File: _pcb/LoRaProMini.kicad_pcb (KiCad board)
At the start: 2 copper layers, 90 x 32 mm, 23 parts, among them U1 MCP1700-3302E_SOT23

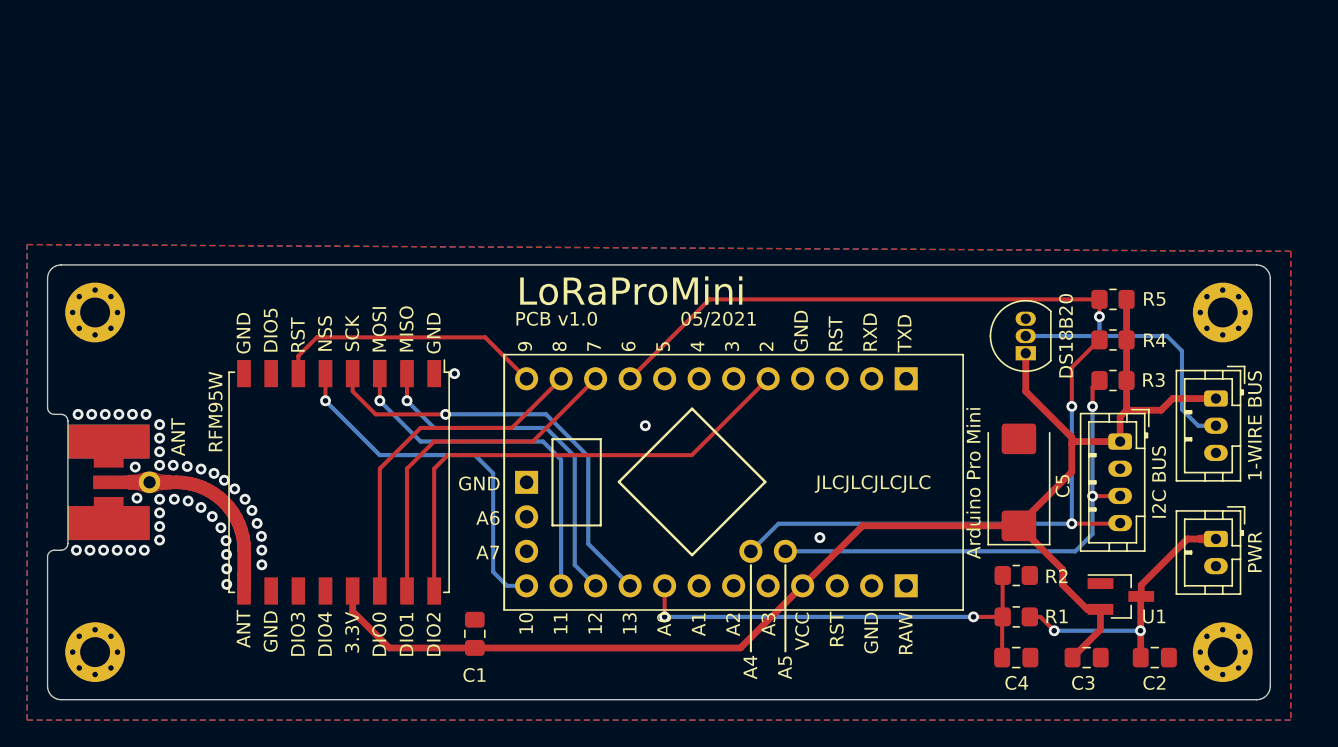
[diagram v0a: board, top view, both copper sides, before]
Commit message: Added REV 2.0 PCB
- Resized PCB
- Fixed DS18x orientation
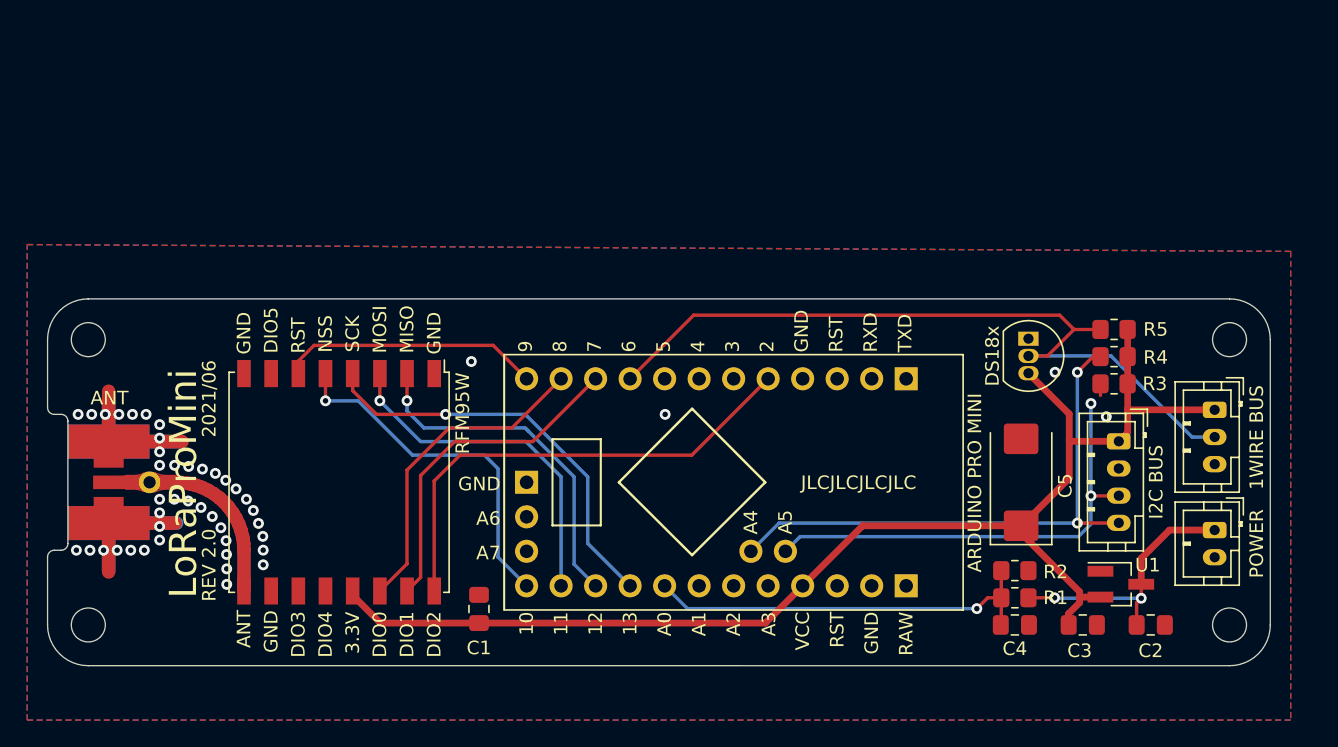
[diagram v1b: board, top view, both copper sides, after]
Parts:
- C1: value C -> 10uF
- C4: value C -> 100nF
- J2: renamed from 1-WIRE BUS
- J3: renamed from I2C BUS
- R1: value R -> 10M
- R2: value R -> 2.7M
- REF** (x4): value MountingHole_2.2mm_M2_Pad_Via -> MountingHole_2.5mm; footprint MountingHole:MountingHole_2.2mm_M2_Pad_Via -> MountingHole:MountingHole_2.5mm
- X1: renamed from Arduino Pro Mini; value Arduino_Pro_Mini -> ARDUINO_PRO_MINI
- moved C2 2.42 mm to (180.1, 101.2)
- moved C3 2.42 mm to (175.1, 101.2)
- moved C4 2.40 mm to (170.1, 101.2)
- moved R5 2.21 mm to (177.4, 79.4)
- moved REF** 2.06 mm to (185.9, 101.2)
- moved REF** 2.06 mm to (101.9, 101.2)
- moved REF** 2.06 mm to (101.9, 80.2)
- moved REF** 2.06 mm to (185.9, 80.2)
- moved C1 1.86 mm to (130.7, 100.0), turned to 90 degrees
- moved R1 1.41 mm to (170.1, 99.2)
- moved R4 1.23 mm to (177.4, 81.4)
- moved U3 1.09 mm to (171.1, 80.1), turned to 270 degrees
- moved U1 0.90 mm to (177.9, 98.2)
- moved J2 0.84 mm to (184.8, 85.4)
- moved J1 0.66 mm to (184.8, 94.2)
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- renumbered ANT to AE1, PWR to J1, RFM95W to U2, DS18B20 to U3
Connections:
- C1 pad 1: GND -> +3V3
- C1 pad 2: +3V3 -> GND
- U3 pad 1: +3V3 -> GND
- U3 pad 3: GND -> +3V3
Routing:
- net GND: track 3.94 -> 36.0 mm, vias 46 -> 45
- net +3V3: track 107.8 -> 98.8 mm
- net MCU_A0: track 33.2 -> 29.8 mm, vias 2 -> 1
- net 1-WIRE: track 59.5 -> 57.3 mm, vias 1 -> 0
- net MCU_SCL: track 36.7 -> 35.1 mm
- net LORA_DIO0: track 25.1 -> 23.9 mm
- net +BATT: track 20.9 -> 19.7 mm
- net MCU_SDA: track 42.4 -> 41.2 mm
- net SPI_SCK: track 31.4 -> 30.6 mm
- net SPI_MOSI: track 26.4 -> 25.7 mm
- net LORA_RST: track 19.9 -> 19.2 mm
- net LORA_DIO1: track 25.6 -> 24.9 mm
- net LORA_DIO2: track 36.3 -> 35.8 mm
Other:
- board size 90 x 32 mm -> 90 x 27 mm
- board text added: "1WIRE BUS"
- board text added: "2021/06"
- board text added: "ANT"
- board text added: "ARDUINO PRO MINI"
- board text added: "DS18x"
- board text added: "I2C BUS"
- board text added: "POWER"
- board text added: "REV 2.0"
- board text added: "RFM95W"
- board text added: "github.com/foorschtbar/LoRaProMini"
- board text removed: "05/2021"
- board text removed: "PCB v1.0"
- board text removed: "https://github.com/foorschtbar/LoRaProMini"

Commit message: Added REV 2.1 PCB
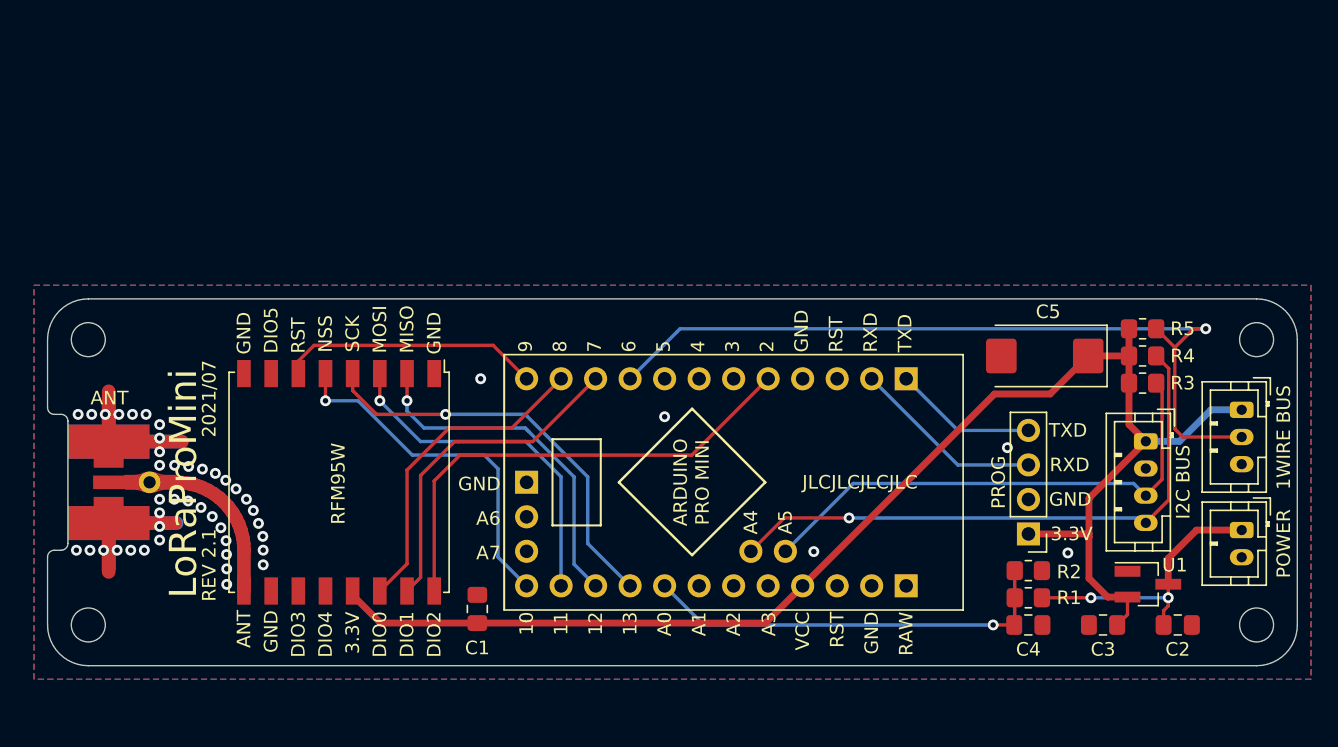
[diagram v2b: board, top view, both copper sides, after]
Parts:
- removed U3: DS18B20, Package_TO_SOT_THT:TO-92_Inline
- added J4: Conn_01x04, Connector_PinHeader_2.54mm:PinHeader_1x04_P2.54mm_Vertical, F.Cu at (171.1, 94.5)
- R3, R4, R5: value 4,7k -> 4,7K
- X1: value ARDUINO_PRO_MINI -> Arduino_Pro_Mini
- moved C5 9.46 mm to (172.3, 81.4), turned to 180 degrees
- moved R3 2.10 mm to (179.5, 83.4), turned to 180 degrees
- moved R4 2.10 mm to (179.5, 81.4), turned to 0 degrees
- moved R5 2.10 mm to (179.5, 79.4), turned to 0 degrees
- moved C2 1.99 mm to (182.1, 101.2)
- moved J1 1.99 mm to (186.8, 94.2)
- moved J2 1.99 mm to (186.8, 85.4)
- moved REF** 1.99 mm to (187.9, 101.2)
- moved REF** 1.99 mm to (187.9, 80.2)
- moved U1 1.99 mm to (179.9, 98.2)
- moved J3 1.99 mm to (179.8, 87.7)
- moved C3 1.49 mm to (176.6, 101.2), turned to 180 degrees
- moved C4 0.99 mm to (171.1, 101.2)
- moved R1 0.99 mm to (171.1, 99.2)
- moved R2 0.99 mm to (171.1, 97.2)
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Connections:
- X1 pad 1: Net-(X1-Pad1) -> TXD
- X1 pad 2: Net-(X1-Pad2) -> RXD
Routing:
- net RXD: track 0.00 -> 14.2 mm
- net TXD: track 0.00 -> 10.6 mm
- net +3V3: track 98.8 -> 108.3 mm
- net MCU_SCL: track 35.1 -> 38.0 mm, vias 2 -> 0
- net GND: track 36.0 -> 38.8 mm, vias 45 -> 46
- net 1-WIRE: track 57.3 -> 59.8 mm, vias 0 -> 1
- net MCU_SDA: track 41.2 -> 43.5 mm, vias 2 -> 1
- net MCU_A0: track 29.8 -> 30.9 mm
- net +BATT: track 19.7 -> 20.6 mm
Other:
- board size 90 x 27 mm -> 92 x 27 mm
- board text added: "2021/07"
- board text added: "PROG"
- board text added: "REV 2.1"
- board text added: "RXD"
- board text added: "TXD"
- board text removed: "2021/06"
- board text removed: "DS18x"
- board text removed: "REV 2.0"

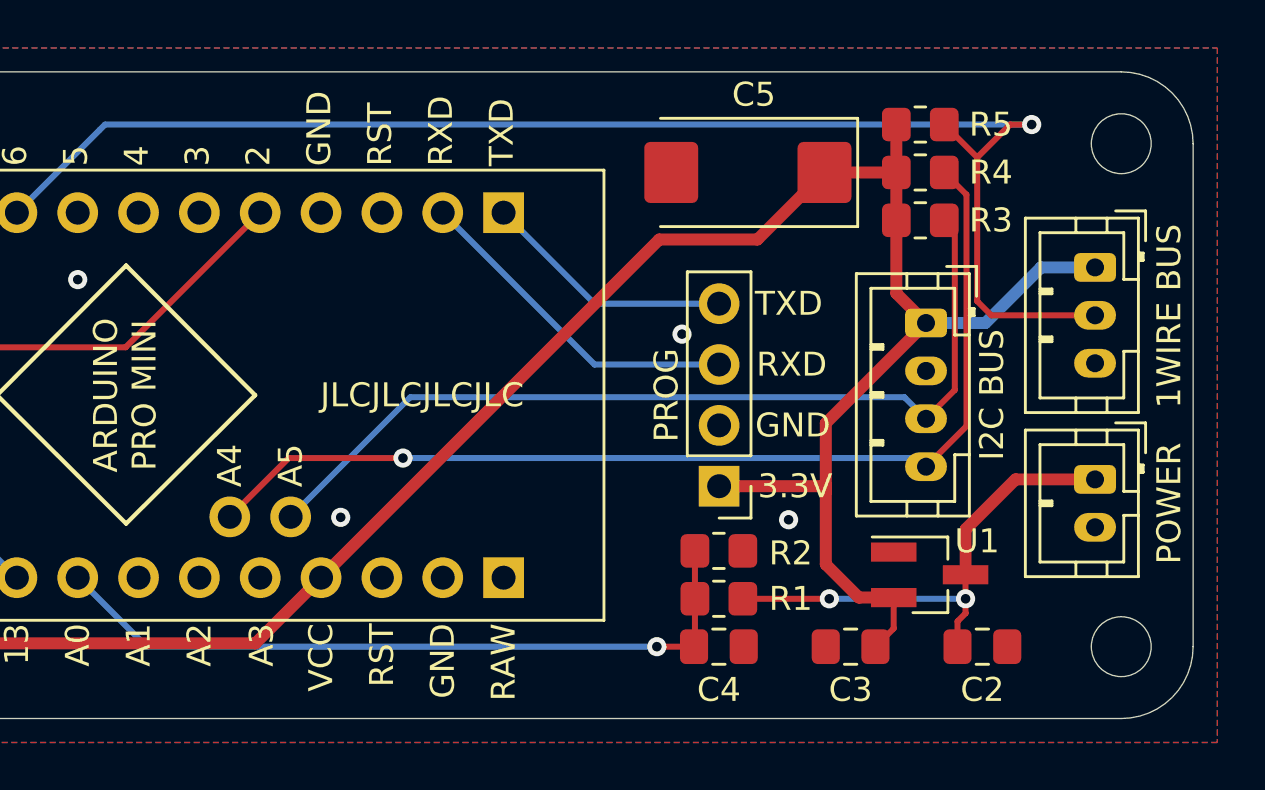
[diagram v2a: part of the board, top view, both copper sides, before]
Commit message: Replaced REV 2.1 PCB
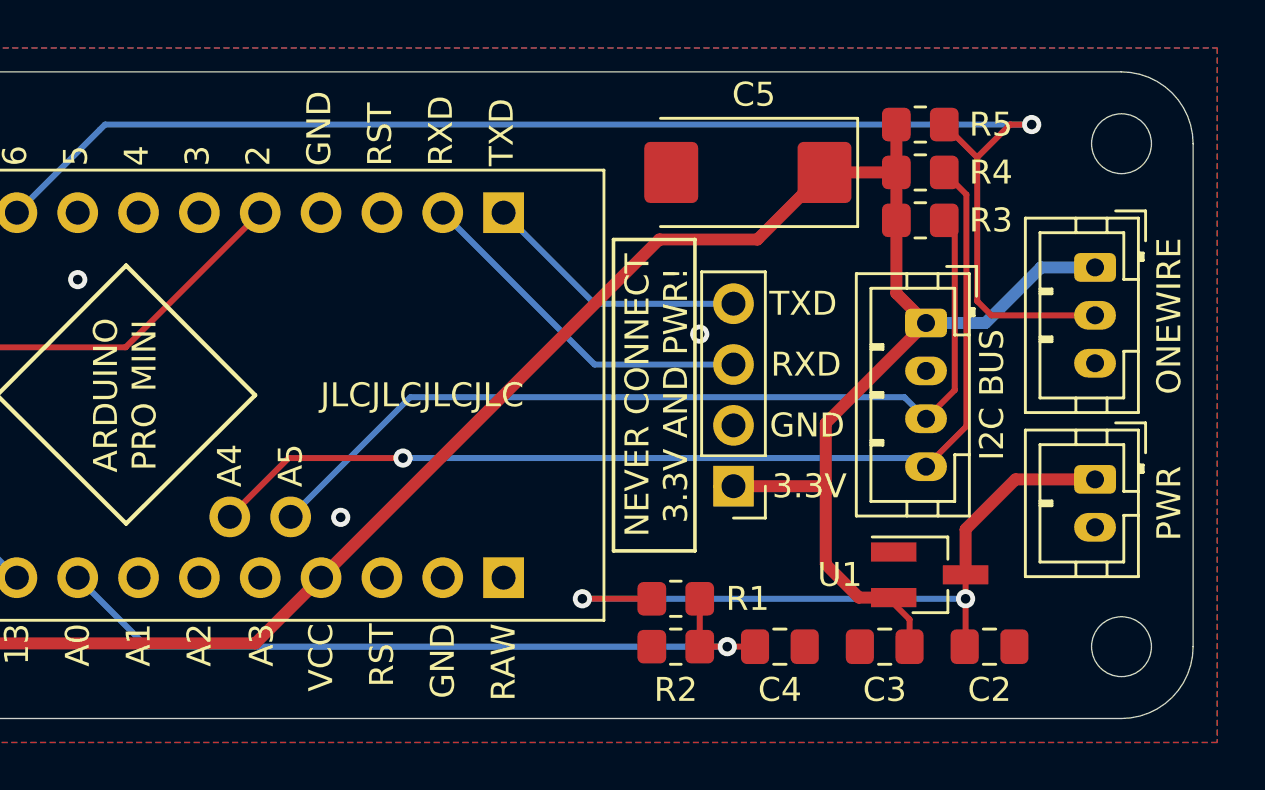
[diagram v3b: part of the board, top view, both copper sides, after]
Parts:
- moved R2 4.39 mm to (169.3, 101.2), turned to 0 degrees
- moved C4 2.55 mm to (173.7, 101.2)
- moved R1 1.80 mm to (169.3, 99.2), turned to 180 degrees
- moved C3 1.42 mm to (178.1, 101.2)
- moved J4 0.60 mm to (171.7, 94.5)
- moved C2 0.30 mm to (182.4, 101.2)
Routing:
- net +BATT: track 20.6 -> 30.1 mm
- net MCU_A0: track 30.9 -> 32.8 mm
- net GND: vias 46 -> 45
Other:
- board text added: "NEVER CONNECT 3.3V AND PWR!"
- board text added: "ONEWIRE"
- board text added: "PWR"
- board text added: "VIN MAX 6.0V!"
- board text removed: "1WIRE BUS"
- board text removed: "POWER"
- board text removed: "PROG"

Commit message: WIP
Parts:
- removed X1: Arduino_Pro_Mini, foorschtbar:Arduino_Pro_Mini
- added C6: 0.1uF, Capacitor_SMD:C_0805_2012Metric_Pad1.18x1.45mm_HandSolder, F.Cu at (130.9, 96.7)
- added C7: 10uF, Capacitor_SMD:C_0805_2012Metric_Pad1.18x1.45mm_HandSolder, F.Cu at (146.9, 98.7)
- added J5: Conn_01x05, Connector_PinHeader_2.54mm:PinHeader_1x05_P2.54mm_Vertical, F.Cu at (131.4, 79.7)
- added J6: Conn_01x08, Connector_PinHeader_2.54mm:PinHeader_1x08_P2.54mm_Vertical, F.Cu at (131.4, 101.7)
- added R6: 10K, Resistor_SMD:R_0805_2012Metric_Pad1.20x1.40mm_HandSolder, F.Cu at (146.9, 96.7)
- added SW1: SW_Push, Button_Switch_SMD:SW_SPST_CK_RS282G05A3, F.Cu at (146.9, 90.7)
- added U4: ATmega328P-AU, Package_QFP:TQFP-32_7x7mm_P0.8mm, F.Cu at (136.9, 90.7)
- added Y1: Resonator, Crystal:Resonator_SMD_muRata_CSTxExxV-3Pin_3.0x1.1mm, F.Cu at (142.4, 84.7)
- J4: value Conn_01x04 -> Conn_01x05; footprint Connector_PinHeader_2.54mm:PinHeader_1x04_P2.54mm_Vertical -> Connector_PinHeader_2.54mm:PinHeader_1x05_P2.54mm_Vertical
- moved R3 39.7 mm to (142.9, 98.7)
- moved R4 39.7 mm to (142.9, 96.7)
- moved R5 29.3 mm to (157.9, 99.2)
- moved C2 16.0 mm to (166.4, 101.2)
- moved C3 16.0 mm to (162.1, 101.2)
- moved C4 16.0 mm to (157.7, 101.2)
- moved J1 16.0 mm to (170.8, 94.2)
- moved J2 16.0 mm to (170.8, 85.4)
- moved J3 16.0 mm to (163.8, 87.7)
- moved R1 16.0 mm to (153.3, 99.2)
- moved R2 16.0 mm to (153.3, 101.2)
- moved REF** 16.0 mm to (171.9, 101.2)
- moved REF** 16.0 mm to (171.9, 80.2)
- moved U1 16.0 mm to (163.9, 98.2)
- moved C5 15.6 mm to (156.7, 81.2)
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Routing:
- net +3V3: track 108.3 -> 0.00 mm
- net 1-WIRE: track 59.8 -> 0.00 mm, vias 1 -> 0
- net MCU_SDA: track 43.5 -> 0.00 mm, vias 1 -> 0
- net MCU_SCL: track 38.0 -> 0.00 mm
- net LORA_DIO2: track 35.8 -> 0.00 mm
- net MCU_A0: track 32.8 -> 0.00 mm, vias 1 -> 0
- net GND: track 38.8 -> 7.30 mm, vias 45 -> 0
- net SPI_SCK: track 30.6 -> 0.00 mm, vias 1 -> 0
- net +BATT: track 30.1 -> 0.00 mm, vias 2 -> 0
- net SPI_CS_LORA: track 26.3 -> 0.00 mm, vias 1 -> 0
- net SPI_MISO: track 26.0 -> 0.00 mm, vias 1 -> 0
- net SPI_MOSI: track 25.7 -> 0.00 mm, vias 1 -> 0
- net LORA_DIO1: track 24.9 -> 0.00 mm
- net LORA_DIO0: track 23.9 -> 0.00 mm
- net LORA_RST: track 19.2 -> 0.00 mm
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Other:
- board size 92 x 27 mm -> 76 x 27 mm
- board text added: "RST"
- board text removed: "ARDUINO PRO MINI"

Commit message: WIP
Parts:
- removed the REF** at (171.9, 101.2)
- removed the REF** at (171.9, 80.2)
- added REF**: MountingHole_2.5mm, MountingHole:MountingHole_2.5mm, F.Cu at (167.9, 101.2)
- added REF**: MountingHole_2.5mm, MountingHole:MountingHole_2.5mm, F.Cu at (167.9, 80.2)
- U1: footprint Package_TO_SOT_SMD:SOT-23_Handsoldering -> Package_TO_SOT_SMD:SOT-23
- moved C2 29.9 mm to (143.0, 82.7)
- moved R1 27.8 mm to (130.9, 82.7)
- moved R2 27.8 mm to (130.9, 84.7)
- moved C3 22.4 mm to (146.9, 84.7)
- moved C4 20.9 mm to (136.9, 98.7)
- moved R5 20.9 mm to (142.9, 84.7)
- moved J2 14.0 mm to (160.4, 94.7)
- moved U1 9.81 mm to (154.4, 100.7), turned to 180 degrees
- moved C5 6.32 mm to (150.4, 80.7)
- moved J1 6.30 mm to (166.4, 89.7)
- moved Y1 5.85 mm to (136.9, 82.7), turned to 180 degrees
- moved J3 5.59 mm to (160.4, 83.2)
- moved J4 3.00 mm to (154.4, 95.8)
- moved SW1 1.00 mm to (145.9, 90.7), turned to 90 degrees
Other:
- board size 76 x 27 mm -> 72 x 27 mm
- board text added: "1-WIRE"
- board text added: "I2C"
- board text removed: "I2C BUS"
- board text removed: "ONEWIRE"

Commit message: WIP
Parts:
- added J7: Conn_01x02, Connector_JST:JST_PH_B2B-PH-K_1x02_P2.00mm_Vertical, F.Cu at (160.0, 91.7)
- added J8: Conn_01x02, Connector_JST:JST_PH_B2B-PH-K_1x02_P2.00mm_Vertical, F.Cu at (160.0, 99.2)
- added R7: 4,7K, Resistor_SMD:R_0805_2012Metric_Pad1.20x1.40mm_HandSolder, F.Cu at (154.2, 99.7)
- added R8: 4,7K, Resistor_SMD:R_0805_2012Metric_Pad1.20x1.40mm_HandSolder, F.Cu at (154.2, 101.7)
- J5: footprint Connector_PinHeader_2.54mm:PinHeader_1x05_P2.54mm_Vertical -> foorschtbar:Holes_1x05_P2.54mm
- J6: footprint Connector_PinHeader_2.54mm:PinHeader_1x08_P2.54mm_Vertical -> foorschtbar:Holes_1x08_P2.54mm
- moved REF** 36.1 mm to (138.3, 126.4)
- moved U1 21.3 mm to (154.7, 79.4), turned to 0 degrees
- moved C2 11.8 mm to (154.7, 82.4)
- moved J2 7.02 mm to (167.0, 92.3)
- moved J1 4.64 mm to (167.0, 85.1)
- moved J3 3.03 mm to (160.0, 80.2)
- moved C5 2.38 mm to (148.1, 80.1)
- moved J5 0.50 mm to (131.4, 79.2)
- moved J6 0.50 mm to (131.4, 102.2)
- moved Y1 0.30 mm to (136.9, 83.0)
- moved C3 0.10 mm to (146.9, 84.8)
- moved R2 0.10 mm to (130.9, 84.8)
- moved R5 0.10 mm to (142.9, 84.8)
- moved C6 0.10 mm to (130.9, 96.6)
- moved R4 0.10 mm to (142.9, 96.6)
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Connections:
- net MCU_A0 renamed MCU_A0_BAT
- net RXD renamed MCU_RXD
- net TXD renamed MCU_TXD
- C7 pad 1: RST -> MCU_RST
- J4 pad 5: RST -> MCU_RST
- J6 pad 3: MCU_A2 -> MCU_A3
- J6 pad 4: MCU_A3 -> MCU_A6
- J6 pad 5: MCU_A6 -> MCU_A7
- J6 pad 6: MCU_A7 -> MCU_RST
- R5 pad 1: +3V3 -> 1-WIRE
- R5 pad 2: 1-WIRE -> +3V3
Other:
- board text added: "2021/09"
- board text added: "A1"
- board text added: "A2"
- board text added: "A3"
- board text added: "A6"
- board text added: "A7"
- board text added: "D3"
- board text added: "D4"
- board text added: "D5"
- board text added: "RESET"
- board text added: "REV 3.0"
- board text added: "VCC"
- board text removed: "NEVER CONNECT 3.3V AND PWR!"
- board text removed: "REV 2.1"

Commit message: WIP
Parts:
- added REF**: OSHW-Logo2_7.3x6mm_SilkScreen, Symbol:OSHW-Logo2_7.3x6mm_SilkScreen, B.Cu at (126.8, 90.8)
- added REF**: ESD-Logo_6.6x6mm_SilkScreen, Symbol:ESD-Logo_6.6x6mm_SilkScreen, F.Cu at (120.4, 90.6)
- moved REF** 35.7 mm to (138.4, 90.7)
- moved J7 7.50 mm to (160.0, 99.2)
- moved J8 7.50 mm to (160.0, 91.7)
- moved R3 2.10 mm to (142.9, 96.6)
- moved R4 2.10 mm to (142.9, 98.7)
- moved R7 2.00 mm to (154.2, 101.7)
- moved R8 2.00 mm to (154.2, 99.7)
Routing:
- net +3V3: track 0.00 -> 170.7 mm, vias 0 -> 1
- net MCU_D3: track 0.00 -> 52.9 mm, vias 0 -> 3
- net MCU_D4: track 0.00 -> 47.5 mm, vias 0 -> 2
- net 1-WIRE: track 0.00 -> 43.5 mm, vias 0 -> 2
- net +BATT: track 0.00 -> 43.4 mm, vias 0 -> 2
- net MCU_SDA: track 0.00 -> 34.1 mm, vias 0 -> 1
- net MCU_SCL: track 0.00 -> 30.3 mm, vias 0 -> 1
- net MCU_RST: track 0.00 -> 22.9 mm, vias 0 -> 2
- net MCU_A0_BAT: track 0.00 -> 22.1 mm, vias 0 -> 3
- net LORA_RST: track 0.00 -> 21.3 mm, vias 0 -> 2
- net LORA_DIO2: track 0.00 -> 20.4 mm, vias 0 -> 2
- net SPI_CS_LORA: track 0.00 -> 18.8 mm, vias 0 -> 2
- net LORA_DIO0: track 0.00 -> 18.4 mm, vias 0 -> 2
- net LORA_DIO1: track 0.00 -> 18.3 mm, vias 0 -> 2
- net SPI_SCK: track 0.00 -> 17.1 mm
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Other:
- board text added: "MAX 6V!"
- board text added: "MEGA328P"
- board text removed: "2021/07"
- board text removed: "ANT"
- board text removed: "VIN MAX 6.0V!"

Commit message: WIP
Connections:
- J8 pad 2: MCU_D4 -> MCU_D5
- R8 pad 1: MCU_D4 -> MCU_D5
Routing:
- net MCU_D5: track 7.77 -> 47.2 mm, vias 1 -> 3
- net MCU_D4: track 47.5 -> 16.6 mm, vias 2 -> 1
- net 1-WIRE: track 43.5 -> 48.2 mm
- net +3V3: track 170.7 -> 174.6 mm
- net MCU_D3: track 52.9 -> 55.0 mm
- net GND: track 7.30 -> 9.19 mm, vias 22 -> 28
- net LORA_DIO2: track 20.4 -> 19.0 mm
- net MCU_A0_BAT: track 22.1 -> 21.8 mm, vias 3 -> 2
